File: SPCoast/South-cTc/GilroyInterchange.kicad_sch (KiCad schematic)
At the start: 1 part

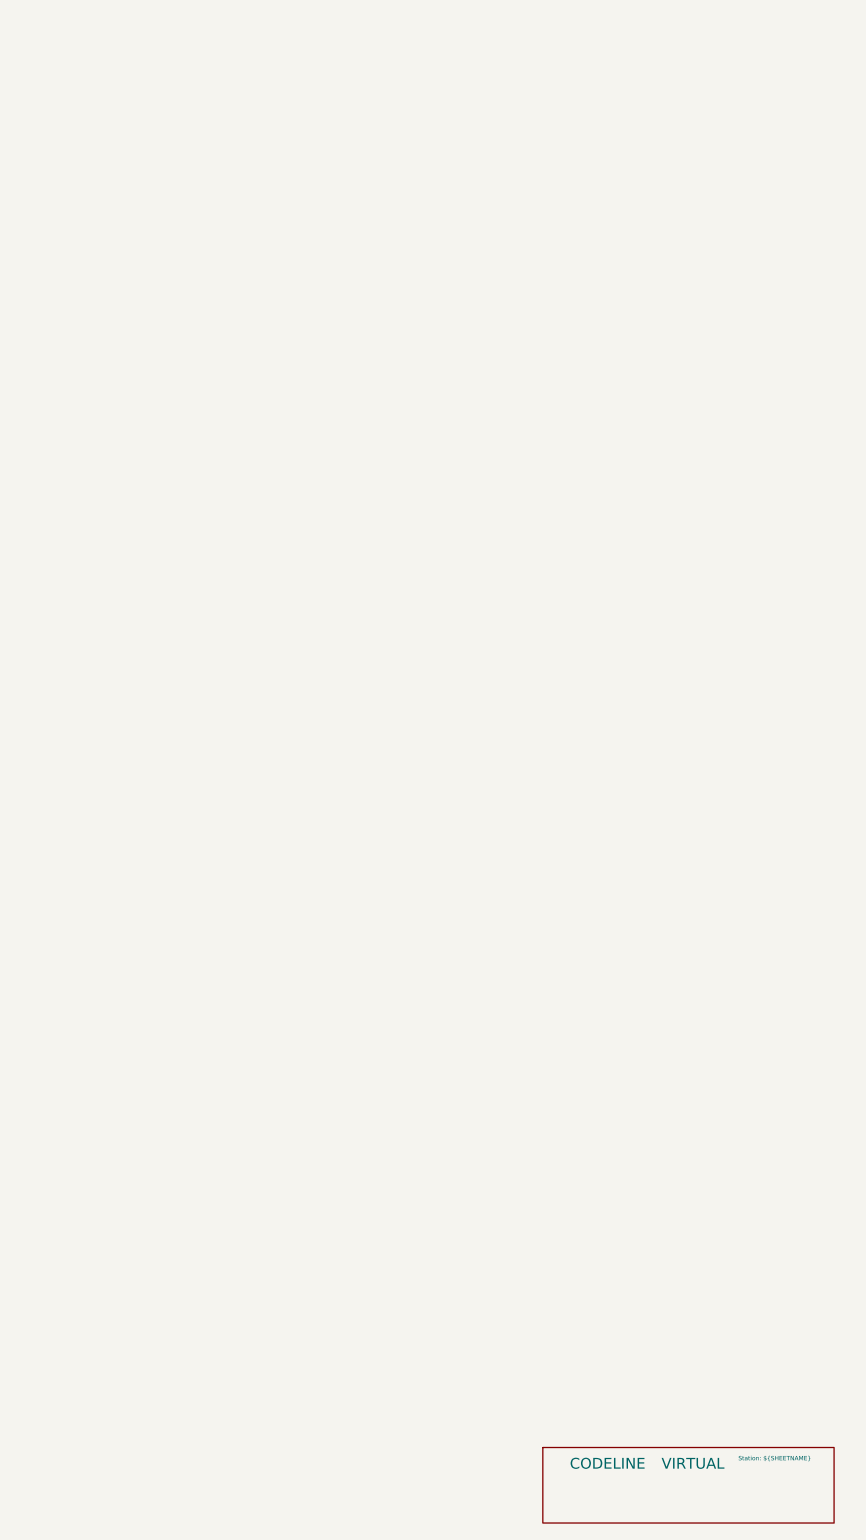
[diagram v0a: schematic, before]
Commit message: SPCoast: derail pin R, track circuit names end in T, code line symbols on the root sheet
Working-tree changes from the 2026-10-01..03 vocabulary review with
FieldUnit-Subdivision (docs/adr/0001-code-line-type-contract.md):

- Switch_Powered_Derail pin 2 is R (through path = REVERSE) in the seven
  plant schematics (library Railroad.kicad_sym renamed alongside; not in git)
- Luchessa track circuits renamed to end in T (1SAT, 2NAAT, ...); MC1 moved
  to CP Gilroy's house
- South-cTc: transports (MQTT, TimeCode, CMRInet, Loconet) on the root
  sheet on the CtcMachine Transports pin; field stations as encoding
  instances on the Luchessa sheet; two Luchessa lamp tokens renamed
- Six plant projects (Christopher, Corporal, GilroyCalTrain,
  GilroyInterchange, Sargent, Watsonville) added as drawn so far; Watsonville
  updated 2026-10-02

Co-Authored-By: Claude Fable 5.1 <noreply@anthropic.com>
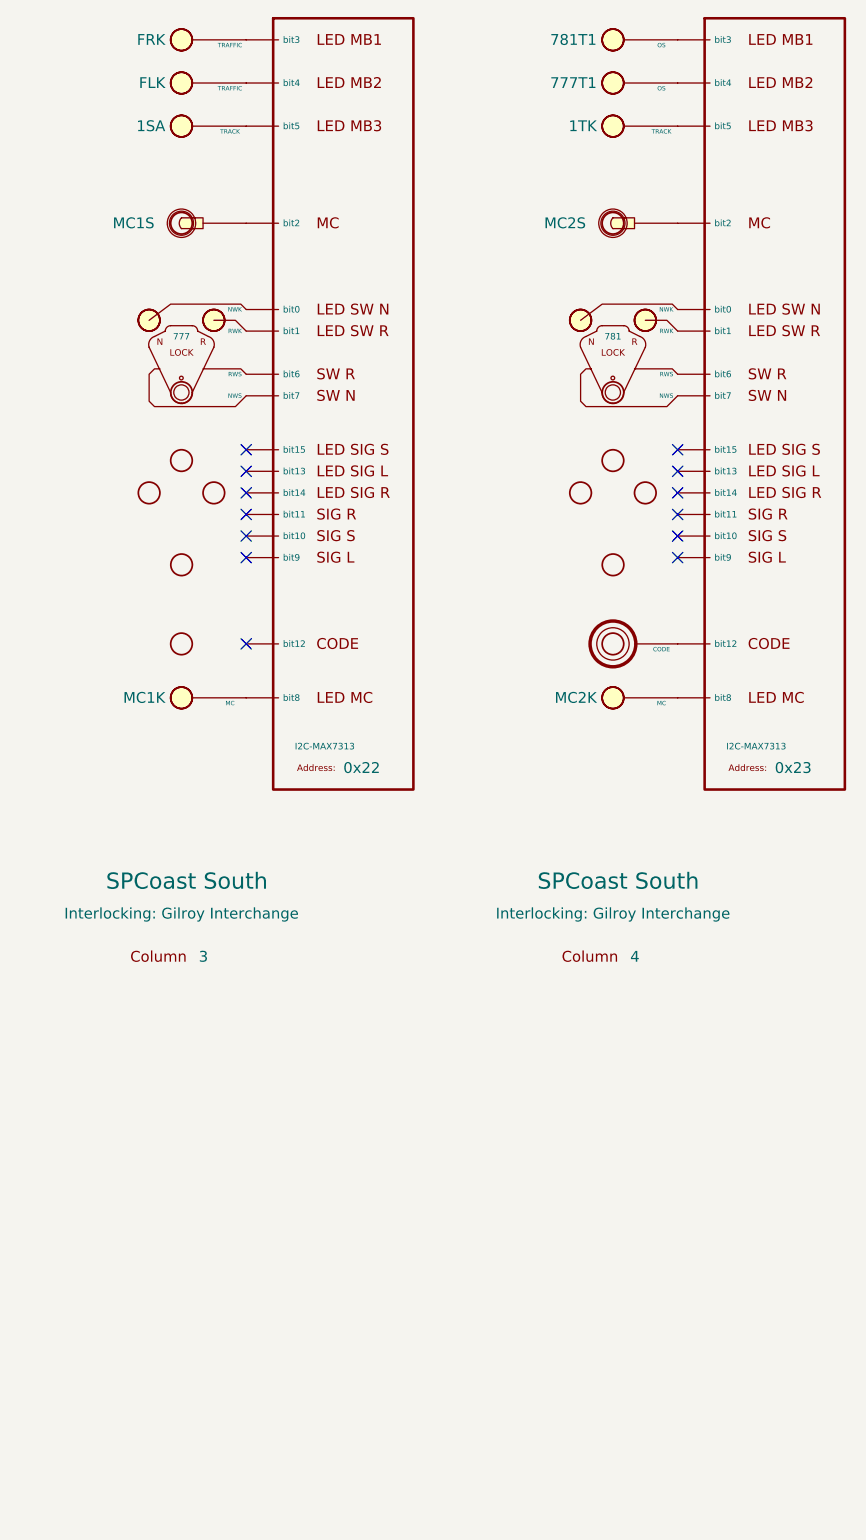
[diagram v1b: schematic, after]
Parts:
- removed CODELINE2: VIRTUAL, symbol RailroadPanel:Codeline-Virtual
- added CDE4: CODE, symbol RailroadPanel:PanelCode
- added COL23: 3, symbol RailroadPanel:PanelColumn
- added COL24: 4, symbol RailroadPanel:PanelColumn
- added LKL3: 777, symbol RailroadPanel:PanelLock
- added LKL4: 781, symbol RailroadPanel:PanelLock
- added LMP31, LMP32: TRAFFIC, symbol RailroadPanel:PanelLamp-BLUE
- added LMP33, LMP43: TRACK, symbol RailroadPanel:PanelLamp-YELLOW
- added LMP41, LMP42: OS, symbol RailroadPanel:PanelLamp-YELLOW
- added MCK3, MCK4: MC, symbol RailroadPanel:PanelLamp-YELLOW
- added MCL3: MC1, symbol RailroadPanel:PanelMCall
- added MCL4: MC2, symbol RailroadPanel:PanelMCall
- added U23: 0x22, symbol RailroadPanel:PanelColumn-MAX7313
- added U24: 0x23, symbol RailroadPanel:PanelColumn-MAX7313
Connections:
- new net: COL24.1 (Column), LMP41.1 (Column)
- new net: LMP41.2 (LAMP), U24.4 (bit3)
- new net: COL23.2 (Column), LMP32.1 (Column)
- new net: LMP32.2 (LAMP), U23.5 (bit4)
- new net: CDE4.1 (Column), COL24.7 (Column)
- new net: CDE4.2 (CODE), U24.13 (bit12)
- new net: COL23.3 (Column), LMP33.1 (Column)
- new net: LMP33.2 (LAMP), U23.6 (bit5)
- new net: COL24.8 (Column), MCK4.1 (Column)
- new net: MCK4.2 (LAMP), U24.9 (bit8)
- new net: COL24.5 (Column), LKL4.1 (Column)
- new net: LKL4.2 (NWS), U24.8 (bit7)
- new net: LKL4.3 (RWS), U24.7 (bit6)
- new net: LKL4.4 (RWK), U24.2 (bit1)
- new net: LKL4.5 (NWK), U24.1 (bit0)
- new net: COL23.5 (Column), LKL3.1 (Column)
- new net: LKL3.2 (NWS), U23.8 (bit7)
- new net: LKL3.3 (RWS), U23.7 (bit6)
- new net: LKL3.4 (RWK), U23.2 (bit1)
- new net: LKL3.5 (NWK), U23.1 (bit0)
- new net: COL24.3 (Column), LMP43.1 (Column)
- new net: LMP43.2 (LAMP), U24.6 (bit5)
- new net: COL24.2 (Column), LMP42.1 (Column)
- new net: COL24.4 (Column), MCL4.1 (Column)
- new net: COL23.4 (Column), MCL3.1 (Column)
- new net: MCL3.2 (SW), U23.3 (bit2)
- new net: COL23.1 (Column), LMP31.1 (Column)
- new net: LMP31.2 (LAMP), U23.4 (bit3)
- new net: COL23.8 (Column), MCK3.1 (Column)
- new net: MCL4.2 (SW), U24.3 (bit2)
- new net: LMP42.2 (LAMP), U24.5 (bit4)
- new net: MCK3.2 (LAMP), U23.9 (bit8)
- no-connect marks 0 -> 13

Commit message: SPCoast: Address field and Kind on PanelColumn-MAX7313; encoding Values; HBA; Watsonville update
Owner's drawing changes of 2026-10-02..03 (FieldUnit-Subdivision ADR 0002 D18
and the owner's responses):

- PanelColumn-MAX7313: the expander address moves from the Value to an
  Address field (Value is ${Address}); BusKind renamed Kind (I2C-MAX7313)
- Luchessa encoding symbols: Value "US&S 506 time-coded DC pulses"
- Sargent: HBD renamed HBA; traffic indications [NSEW]FLK
- Watsonville schematic brought to a usable state
- Luchessa plant: track circuits end in T; MC1 at CP Gilroy's house

Co-Authored-By: Claude Fable 5.1 <noreply@anthropic.com>
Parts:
- LMP31: IndicationToken FRK -> Luchessa:NFLK
- LMP32: IndicationToken FLK -> Luchessa:SFLK
- U23: Address (none) -> 0x22; BusKind I2C-MAX7313 -> (none); Kind (none) -> I2C-MAX7313
- U24: Address (none) -> 0x23; BusKind I2C-MAX7313 -> (none); Kind (none) -> I2C-MAX7313
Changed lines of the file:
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@@
 			)
 		)
-		(property "IndicationToken" "FLK"
+		(property "IndicationToken" "Luchessa:SFLK"
 			(at 78.105 31.75 0)
 			(show_name no)
@@
 			)
 		)
-		(property "IndicationToken" "FRK"
+		(property "IndicationToken" "Luchessa:NFLK"
 			(at 78.105 26.67 0)
 			(show_name no)
@@
 		(property "Value" "0x23"
 			(at 149.86 112.395 0)
+			(hide yes)
 			(show_name no)
 			(do_not_autoplace yes)
@@
 			)
 		)
-		(property "BusKind" "I2C-MAX7313"
+		(property "Role" "IODRIVER"
+			(at 148.59 107.315 0)
+			(hide yes)
+			(show_name no)
+			(do_not_autoplace no)
+			(effects
+				(font
+					(size 1.27 1.27)
+				)
+			)
+		)
+		(property "Kind" "I2C-MAX7313"
 			(at 144.145 109.855 0)
 			(show_name no)
-			(do_not_autoplace yes)
+			(do_not_autoplace no)
 			(effects
 				(font
@@
 			)
 		)
-		(property "Role" "IODRIVER"
-			(at 149.86 72.39 0)
-			(hide yes)
+		(property "Address" "0x23"
+			(at 151.892 112.522 0)
 			(show_name no)
 			(do_not_autoplace no)
@@
 		(property "Value" "0x22"
 			(at 99.06 112.395 0)
+			(hide yes)
 			(show_name no)
 			(do_not_autoplace yes)
@@
 			)
 		)
-		(property "BusKind" "I2C-MAX7313"
+		(property "Role" "IODRIVER"
+			(at 97.79 107.315 0)
+			(hide yes)
+			(show_name no)
+			(do_not_autoplace no)
+			(effects
+				(font
+					(size 1.27 1.27)
+				)
+			)
+		)
+		(property "Kind" "I2C-MAX7313"
 			(at 93.345 109.855 0)
 			(show_name no)
-			(do_not_autoplace yes)
+			(do_not_autoplace no)
 			(effects
 				(font
@@
 			)
 		)
-		(property "Role" "IODRIVER"
-			(at 99.06 72.39 0)
-			(hide yes)
-			(show_name no)
-			(do_not_autoplace no)
+		(property "Address" "0x22"
+			(at 101.346 112.522 0)
+			(show_name no)
+			(do_not_autoplace no)

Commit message: fix(kicad): approach circuits end in T; desk tokens follow
Plants: Christopher 1NA/2NA/1SA/2SA, GilroyCalTrain 1NA/1SA, GilroyInterchange
1SA, Sargent 1NA/1SA/2SA gain the final T (ADR 0003 D4). Sargent's reference
Corporal:2NA becomes Corporal:2NAT, the circuit Corporal draws.

Desk (South-cTc sheets): IndicationToken follows the plants for Christopher,
GilroyCalTrain, GilroyInterchange; Corporal 1SA becomes 1SAT (the plant already
had it); Christopher 815T2 becomes 815AT1 (the OS circuit of switch 815A).

Not changed, awaiting decisions in the dry-run report: 0<n>T renames (IND,
TK<n>, Interchange, 2NAAT, 2SAT), section 2 of an approach, unnamed circuits,
Watsonville, CP_Watsonville: references, 1TK.

Verified: netlists rebuilt for all affected projects; of 33 desk circuit tokens,
5 now match no plant circuit (was 11): 1TK, CP_Watsonville:SA1,
CP_Watsonville:837T1, Watsonville 1NAK and 2NAK. KiCad closed, no ~*.lck.

Co-Authored-By: Claude Sonnet 5.5 <noreply@anthropic.com>
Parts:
- LMP33: IndicationToken 1SA -> 1SAT
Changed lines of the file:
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@@
 			)
 		)
-		(property "IndicationToken" "1SA"
+		(property "IndicationToken" "1SAT"
 			(at 78.105 36.83 0)
 			(show_name no)

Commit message: fix(kicad): remaining class I circuits take the 0<n>T form
Owner-approved numbers: Luchessa 2SAT -> 02T; Christopher IND -> 01T;
Corporal IND -> 01T; GilroyInterchange Interchange -> 01T and TK1 -> 02T
(passing-track main and siding merged into class I). Desk lamp 1TK on
GilroyInterchange column 4 becomes 02T.

Verified: netlists rebuilt for the five projects; every 0<n>T is unique within
its plant; desk circuit tokens that match no plant circuit are down to four
(CP_Watsonville:SA1, CP_Watsonville:837T1, Watsonville 1NAK and 2NAK).

Co-Authored-By: Claude Sonnet 5.5 <noreply@anthropic.com>
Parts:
- LMP43: IndicationToken 1TK -> 02T
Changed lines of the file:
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@@
 			)
 		)
-		(property "IndicationToken" "1TK"
+		(property "IndicationToken" "02T"
 			(at 128.905 36.83 0)
 			(show_name no)

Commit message: chore(kicad): refresh instances to the ADR 0003 libraries (InterlockingPlant 95f53e2)
- Desk sheets (South-cTc/*) and the Sargent sandbox: embedded PanelSwitch, PanelLock,
  PanelSignal, PanelMCall, PanelCode, PanelLamp-*, PanelColumn-MAX7313 definitions refreshed
  from the library (refresh_embedded.py, checked against the pre-pass library: only Description
  text had drifted). Instance Role APPLIANCE -> PANEL (77).
- Plant sheets: powered-switch instance Kind SWITCH_POWERED -> SWITCH_REMOTE (21), matching the
  library (sweep_role_kind_fields.py).

Verified:
- verify_symbol_diff.py: same symbols, lib_ids and positions; only Role/Kind changed.
- Nets unchanged: Christopher 30, Corporal 27, GilroyCalTrain 28, GilroyInterchange 23,
  Luchessa 35, Sargent 61, Watsonville 99, South-cTc 341.
- parse_kicad_plant.py --format text identical before/after for all seven plants.
- Desk compile 75/137/14, diagnostics identical; the 7 desk locks bind WLS/~{WLS}/~{WLK}/WLK
  to the bits that were NWS/RWS/RWK/NWK.
- No sheet or project outside Luchessa carries the copied root UUID.

Co-Authored-By: Claude Opus 5.5 <noreply@anthropic.com>
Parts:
- CDE4, LKL3, LKL4, LMP31, LMP32, LMP33, LMP41, LMP42, LMP43, MCK3, MCK4, MCL3, MCL4: Role APPLIANCE -> PANEL
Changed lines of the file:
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@@
 			)
 		)
-		(property "Role" "APPLIANCE"
+		(property "Role" "PANEL"
 			(at 130.81 24.13 0)
 			(hide yes)
@@
 			)
 		)
-		(property "Role" "APPLIANCE"
+		(property "Role" "PANEL"
 			(at 80.01 34.29 0)
 			(hide yes)
@@
 			)
 		)
-		(property "Role" "APPLIANCE"
+		(property "Role" "PANEL"
 			(at 130.81 90.17 0)
 			(hide yes)
@@
 			)
 		)
-		(property "Role" "APPLIANCE"
+		(property "Role" "PANEL"
 			(at 80.01 34.29 0)
 			(hide yes)
@@
 			)
 		)
-		(property "Role" "APPLIANCE"
+		(property "Role" "PANEL"
 			(at 130.81 101.6 0)
 			(hide yes)
@@
 			)
 		)
-		(property "Role" "APPLIANCE"
+		(property "Role" "PANEL"
 			(at 131.445 74.93 0)
 			(hide yes)
@@
 			)
 		)
-		(property "Role" "APPLIANCE"
+		(property "Role" "PANEL"
 			(at 80.645 74.93 0)
 			(hide yes)
@@
 			)
 		)
-		(property "Role" "APPLIANCE"
+		(property "Role" "PANEL"
 			(at 130.81 34.29 0)
 			(hide yes)
@@
 			)
 		)
-		(property "Role" "APPLIANCE"
+		(property "Role" "PANEL"
 			(at 86.36 44.45 0)
 			(hide yes)
@@
 			)
 		)
-		(property "Role" "APPLIANCE"
+		(property "Role" "PANEL"
 			(at 80.01 29.21 0)
 			(hide yes)
@@
 			)
 		)
-		(property "Role" "APPLIANCE"
+		(property "Role" "PANEL"
 			(at 80.01 101.6 0)
 			(hide yes)
@@
 			)
 		)
-		(property "Role" "APPLIANCE"
+		(property "Role" "PANEL"
 			(at 130.81 29.21 0)
 			(hide yes)
@@
 			)
 		)
-		(property "Role" "APPLIANCE"
+		(property "Role" "PANEL"
 			(at 137.16 44.45 0)
 			(hide yes)

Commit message: chore(kicad): desk sheets to Driver-I2C-MAX7313 and the PanelLock Kind (InterlockingPlant owner review)
- 14 desk expanders: lib_id RailroadPanel:PanelColumn-MAX7313 -> Driver-I2C-MAX7313, embedded
  definition refreshed (pins A1..B8, same numbers and positions).
- 8 PanelLock instances: Kind LOCK_LEVER -> LOCK_LEVER_2LAMP_2CONTACT (7 desk, 1 Sargent sandbox).

Verified:
- verify_symbol_diff.py: only those lib_id and Kind changes.
- South-cTc 341 nets, Sargent 61; desk compile 75/137/14 with bindings identical to e2c1093.

Co-Authored-By: Claude Opus 5.5 <noreply@anthropic.com>
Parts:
- LKL3, LKL4: Kind LOCK_LEVER -> LOCK_LEVER_2LAMP_2CONTACT
- U23, U24: symbol RailroadPanel:PanelColumn-MAX7313 -> RailroadPanel:Driver-I2C-MAX7313
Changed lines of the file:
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@@
 			)
 		)
-		(property "Kind" "LOCK_LEVER"
+		(property "Kind" "LOCK_LEVER_2LAMP_2CONTACT"
 			(at 131.445 73.025 0)
 			(hide yes)
@@
 			)
 		)
-		(property "Kind" "LOCK_LEVER"
+		(property "Kind" "LOCK_LEVER_2LAMP_2CONTACT"
 			(at 80.645 73.025 0)
 			(hide yes)
@@
 	)
 	(symbol
-		(lib_id "RailroadPanel:PanelColumn-MAX7313")
+		(lib_id "RailroadPanel:Driver-I2C-MAX7313")
 		(at 149.86 72.39 0)
 		(unit 1)
@@
 	)
 	(symbol
-		(lib_id "RailroadPanel:PanelColumn-MAX7313")
+		(lib_id "RailroadPanel:Driver-I2C-MAX7313")
 		(at 99.06 72.39 0)
 		(unit 1)
